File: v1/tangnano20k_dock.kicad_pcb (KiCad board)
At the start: 2 copper layers, 136.5 x 73.7 mm, 77 parts, among them J1 Mini-DIN-6, J10 DB15_Female_HighDensity_Mount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, J11 DB9_Male_MountingHoles, J12 DB9_Male_MountingHoles, J13 Conn_02x06_Odd_Even, J2 2x20 Pin Female, J3 Conn_01x20, J4 Conn_01x03_Male, J5 Conn_01x02, J6 RCA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

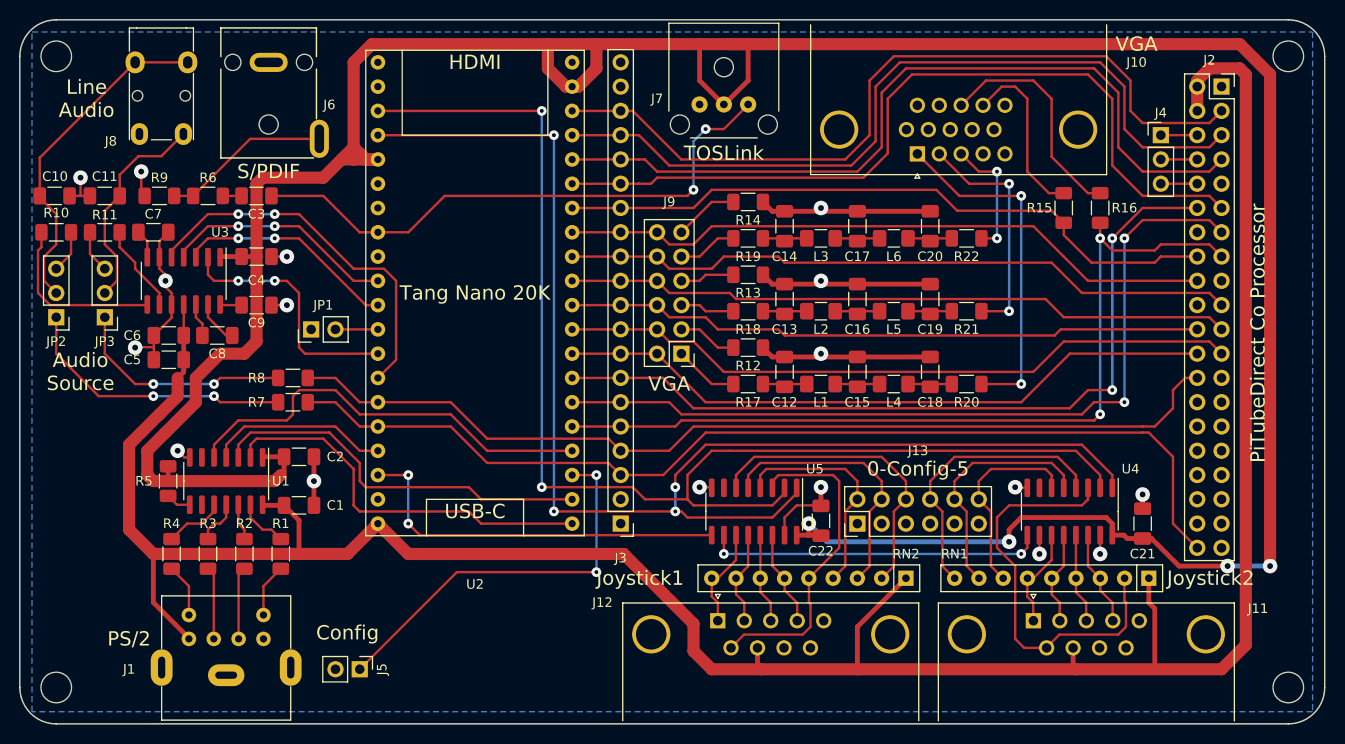
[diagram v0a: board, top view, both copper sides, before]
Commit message: Updated VGA jumper block from 2x6 to 3x6
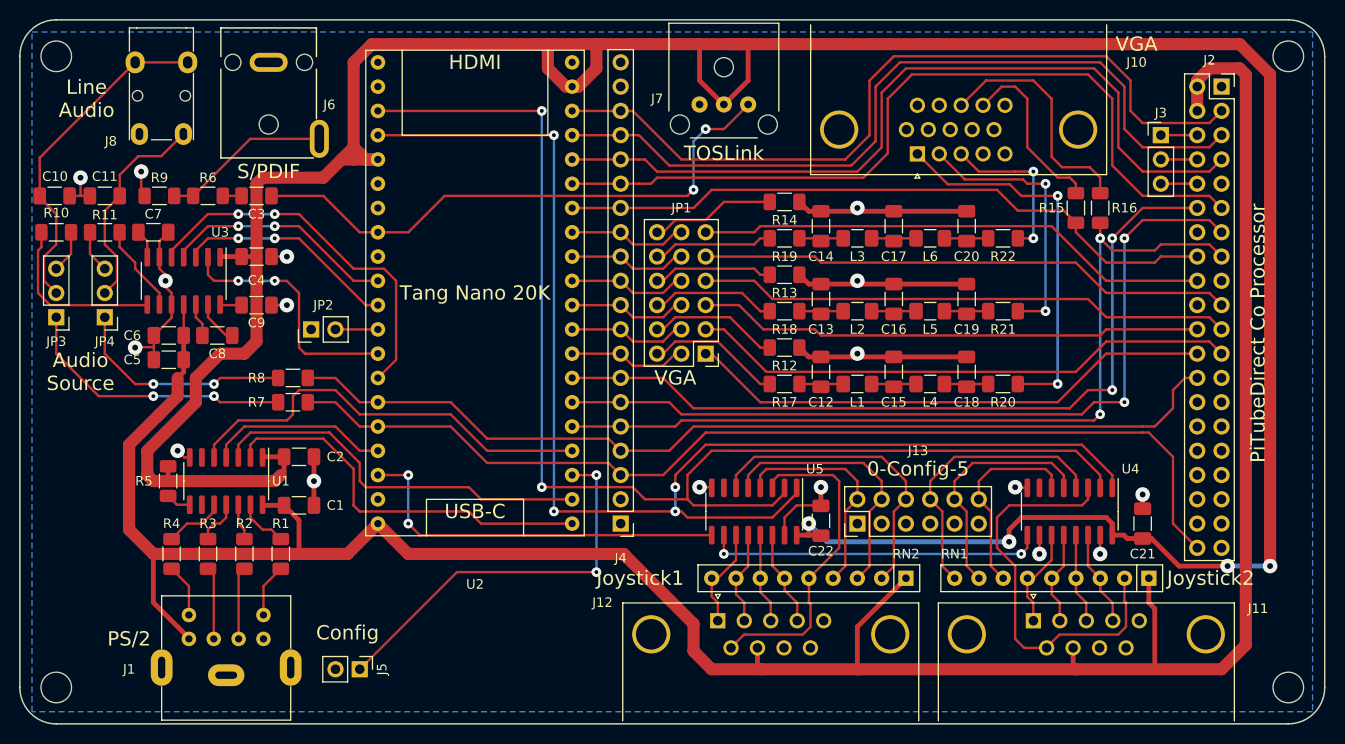
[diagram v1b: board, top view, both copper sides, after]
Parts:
- removed J9: Conn_02x06_Odd_Even, Connector_PinHeader_2.54mm:PinHeader_2x06_P2.54mm_Vertical
- added JP1: Jumper_03x06, TangNano20k:PinHeader_3x06_P2.54mm_Vertical, F.Cu at (144.8, 84.5)
- moved C12 3.81 mm to (156.8, 86.4)
- moved C13 3.81 mm to (156.8, 78.7)
- moved C14 3.81 mm to (156.8, 71.1)
- moved C15 3.81 mm to (164.5, 86.4)
- moved C16 3.81 mm to (164.5, 78.7)
- moved C17 3.81 mm to (164.5, 71.1)
- moved C18 3.81 mm to (172.1, 86.4)
- moved C19 3.81 mm to (172.1, 78.7)
- moved C20 3.81 mm to (172.1, 71.1)
- moved L1 3.81 mm to (160.7, 87.6)
- moved L2 3.81 mm to (160.7, 80.0)
- moved L3 3.81 mm to (160.7, 72.4)
- moved L4 3.81 mm to (168.3, 87.6)
- moved L5 3.81 mm to (168.3, 80.0)
- moved L6 3.81 mm to (168.3, 72.4)
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- renumbered J4 to J3, J3 to J4, JP1 to JP2, JP2 to JP3, JP3 to JP4
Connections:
- J2 pad 18: /VGA_B_n -> /DATA6
- J2 pad 19: /VGA_B -> /DATA2
- J2 pad 21: /VGA_G_n -> /DATA1
- J2 pad 22: /VGA_G -> /DATA7
- J2 pad 23: /VGA_R_n -> /DATA3
- J2 pad 24: /VGA_R -> /DATA0
- R12 pad 1: Net-(J9-Pad3) -> /VGA/VGA_R_n
- R13 pad 1: Net-(J9-Pad7) -> /VGA/VGA_G_n
- R14 pad 1: Net-(J9-Pad11) -> /VGA/VGA_B_n
- R17 pad 1: Net-(J9-Pad1) -> /VGA/VGA_R
- R18 pad 1: Net-(J9-Pad5) -> /VGA/VGA_G
- R19 pad 1: Net-(J9-Pad9) -> /VGA/VGA_B
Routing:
- net /VGA_R_n: track 71.6 -> 11.8 mm
- net /VGA_B: track 71.1 -> 11.8 mm
- net /VGA_R: track 69.6 -> 11.8 mm
- net /DATA3: track 0.00 -> 57.7 mm
- net /VGA_G_n: track 70.0 -> 12.5 mm
- net /VGA_B_n: track 69.1 -> 11.8 mm
- net /DATA2: track 0.00 -> 56.1 mm
- net /DATA1: track 0.00 -> 56.1 mm
- net /VGA_G: track 67.0 -> 11.8 mm
- net /DATA0: track 0.00 -> 55.0 mm
- net /DATA6: track 0.00 -> 54.1 mm
- net /DATA7: track 0.00 -> 53.0 mm
- net /VGA/VGA_R: track 0.00 -> 13.5 mm
- net /VGA/VGA_R_n: track 0.00 -> 13.0 mm
- net /VGA/VGA_B_n: track 0.00 -> 12.5 mm
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
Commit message: Updated VGA jumper block from 3x6 to 3x8
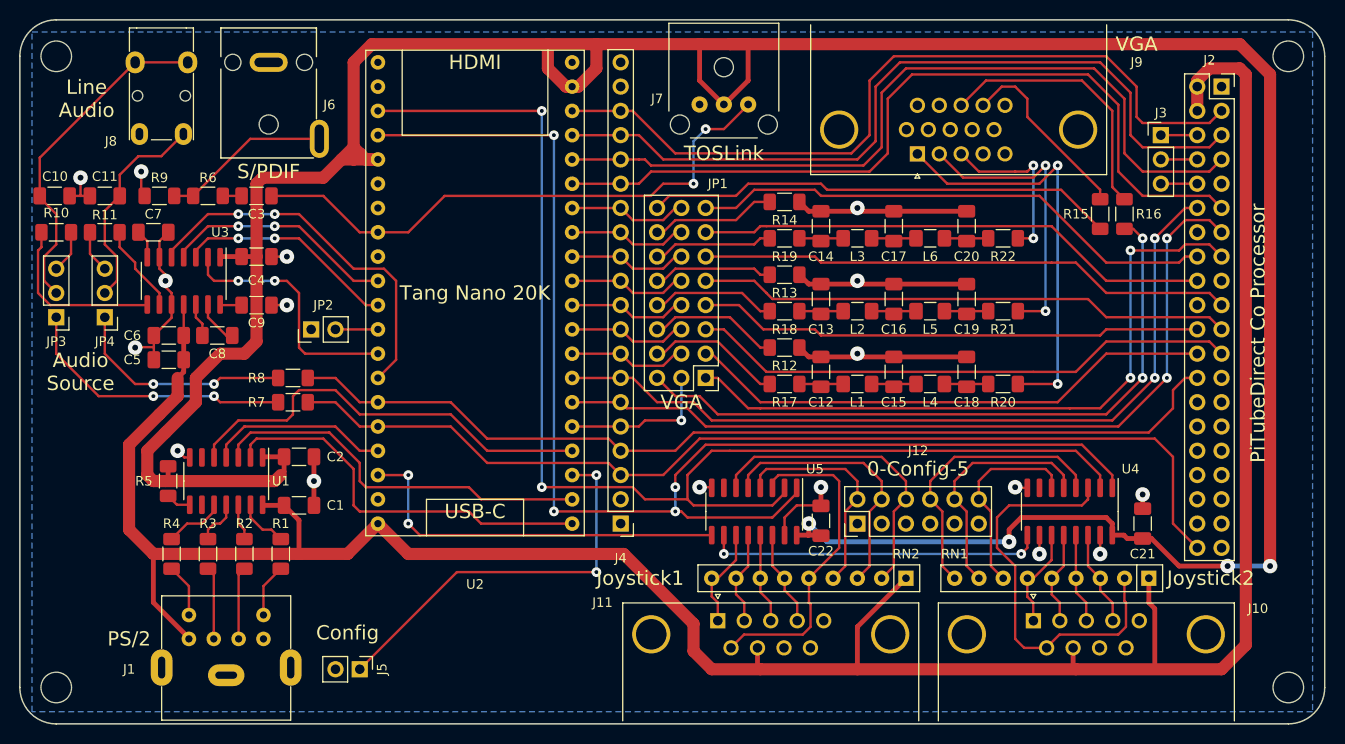
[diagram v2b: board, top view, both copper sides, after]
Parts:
- JP1: value Jumper_03x06 -> Jumper_03x08; footprint TangNano20k:PinHeader_3x06_P2.54mm_Vertical -> TangNano20k:PinHeader_3x08_P2.54mm_Vertical
- moved R15 2.62 mm to (186.1, 69.8)
- moved R16 2.62 mm to (188.6, 69.8)
- moved JP1 2.54 mm to (144.8, 87.0)
- renumbered J11 to J10, J12 to J11, J13 to J12, J10 to J9
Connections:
- J2 pad 15: /VGA_HS -> /DATA4
- J2 pad 16: /VGA_VS -> /DATA5
- JP1 pad 1: /DATA0 -> /DATA4
- JP1 pad 10: /VGA_G_n -> /VGA_R
- JP1 pad 11: /VGA_B -> /VGA_R_n
- JP1 pad 12: /VGA_B_n -> /VGA_G
- JP1 pad 13: /VGA/VGA_R -> /VGA_G_n
- JP1 pad 14: /VGA/VGA_R_n -> /VGA_B
- JP1 pad 15: /VGA/VGA_G -> /VGA_B_n
- JP1 pad 16: /VGA/VGA_G_n -> /VGA_VS
- JP1 pad 17: /VGA/VGA_B -> /VGA/VGA_HS
- JP1 pad 18: /VGA/VGA_B_n -> /VGA/VGA_R
- JP1 pad 2: /DATA3 -> /DATA0
- JP1 pad 3: /DATA7 -> /DATA3
- JP1 pad 4: /DATA1 -> /DATA7
- JP1 pad 5: /DATA2 -> /DATA1
- JP1 pad 6: /DATA6 -> /DATA2
- JP1 pad 7: /VGA_R -> /DATA6
- JP1 pad 8: /VGA_R_n -> /DATA5
- JP1 pad 9: /VGA_G -> /VGA_HS
- R15 pad 1: /VGA_VS -> /VGA/VGA_VS
- R16 pad 1: /VGA_HS -> /VGA/VGA_HS
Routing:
- net /VGA_HS: track 89.8 -> 16.1 mm, vias 2 -> 1
- net /VGA/VGA_HS: track 0.00 -> 70.9 mm, vias 0 -> 2
- net /DATA4: track 0.00 -> 70.7 mm, vias 0 -> 2
- net /VGA_VS: track 70.2 -> 11.8 mm
- net /DATA5: track 0.00 -> 55.6 mm
- net /VGA/VGA_VS: track 0.00 -> 49.4 mm
- net Net-(J9-Pad1): track 40.3 -> 43.8 mm
- net Net-(J9-Pad13): track 25.0 -> 28.0 mm
- net Net-(J9-Pad2): track 28.6 -> 30.8 mm
- net Net-(J9-Pad14): track 18.7 -> 19.6 mm
- net Net-(J9-Pad3): track 16.9 -> 17.8 mm
- net /VGA_G_n: track 12.5 -> 11.8 mm
- net /LED5: track 83.1 -> 82.6 mm
- net /LED3: track 84.6 -> 84.1 mm
- net /LED4: track 83.9 -> 83.4 mm
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
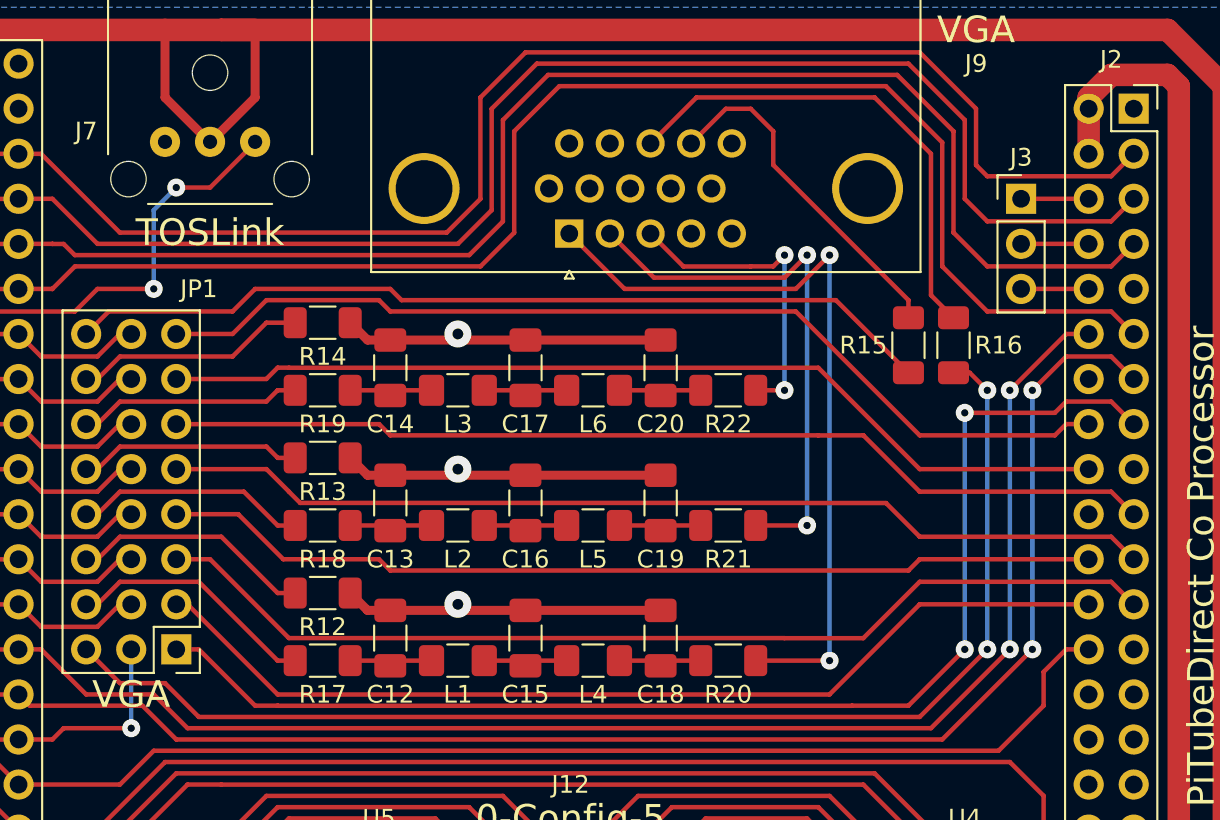
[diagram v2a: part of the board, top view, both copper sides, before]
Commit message: Spread out VGA filter passives
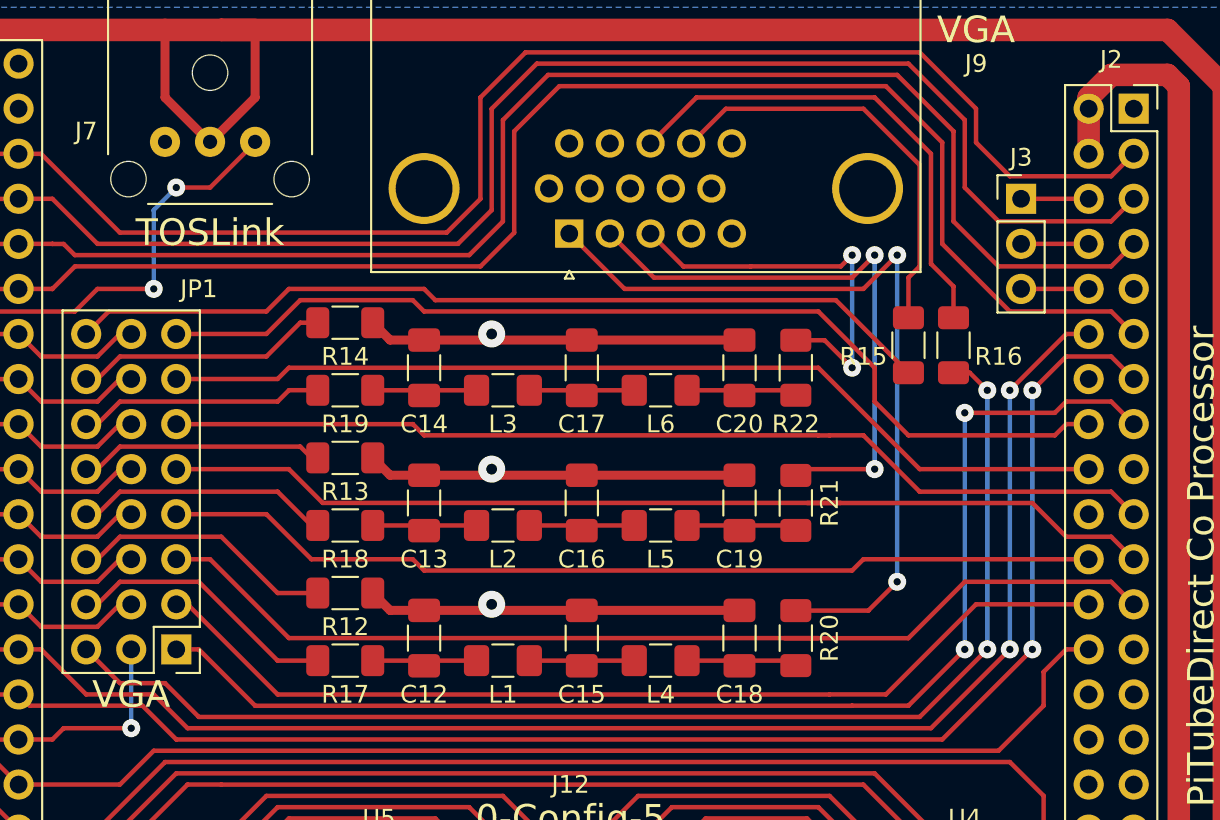
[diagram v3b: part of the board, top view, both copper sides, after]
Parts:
- moved C18 4.44 mm to (176.5, 86.4)
- moved C19 4.44 mm to (176.5, 78.7)
- moved C20 4.44 mm to (176.5, 71.1)
- moved R22 4.02 mm to (179.7, 71.1), turned to 90 degrees
- moved R20 4.02 mm to (179.7, 86.4), turned to 90 degrees
- moved R21 4.02 mm to (179.7, 78.7), turned to 90 degrees
- moved L4 3.81 mm to (172.1, 87.6)
- moved L5 3.81 mm to (172.1, 80.0)
- moved L6 3.81 mm to (172.1, 72.4)
- moved C15 3.17 mm to (167.6, 86.4)
- moved C16 3.17 mm to (167.6, 78.7)
- moved C17 3.17 mm to (167.6, 71.1)
- moved L1 2.54 mm to (163.2, 87.6)
- moved L2 2.54 mm to (163.2, 80.0)
- moved L3 2.54 mm to (163.2, 72.4)
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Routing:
- net GND: track 107.9 -> 117.4 mm
- net Net-(J9-Pad3): track 17.8 -> 22.6 mm
- net Net-(J9-Pad14): track 19.6 -> 23.9 mm
- net /DATA3: track 57.7 -> 59.6 mm
- net /DATA1: track 56.1 -> 58.0 mm
- net Net-(J9-Pad2): track 30.8 -> 32.6 mm
- net Net-(J9-Pad1): track 43.8 -> 45.4 mm
- net Net-(C14-Pad1): track 4.58 -> 5.85 mm
- net Net-(C13-Pad1): track 4.58 -> 5.85 mm
- net Net-(C12-Pad1): track 4.58 -> 5.85 mm
- net Net-(C20-Pad1): track 4.58 -> 5.85 mm
- net Net-(C19-Pad1): track 4.58 -> 5.85 mm
- net Net-(C18-Pad1): track 4.58 -> 5.85 mm
- net Net-(C17-Pad1): track 4.64 -> 5.91 mm
- net Net-(C16-Pad1): track 4.64 -> 5.91 mm
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
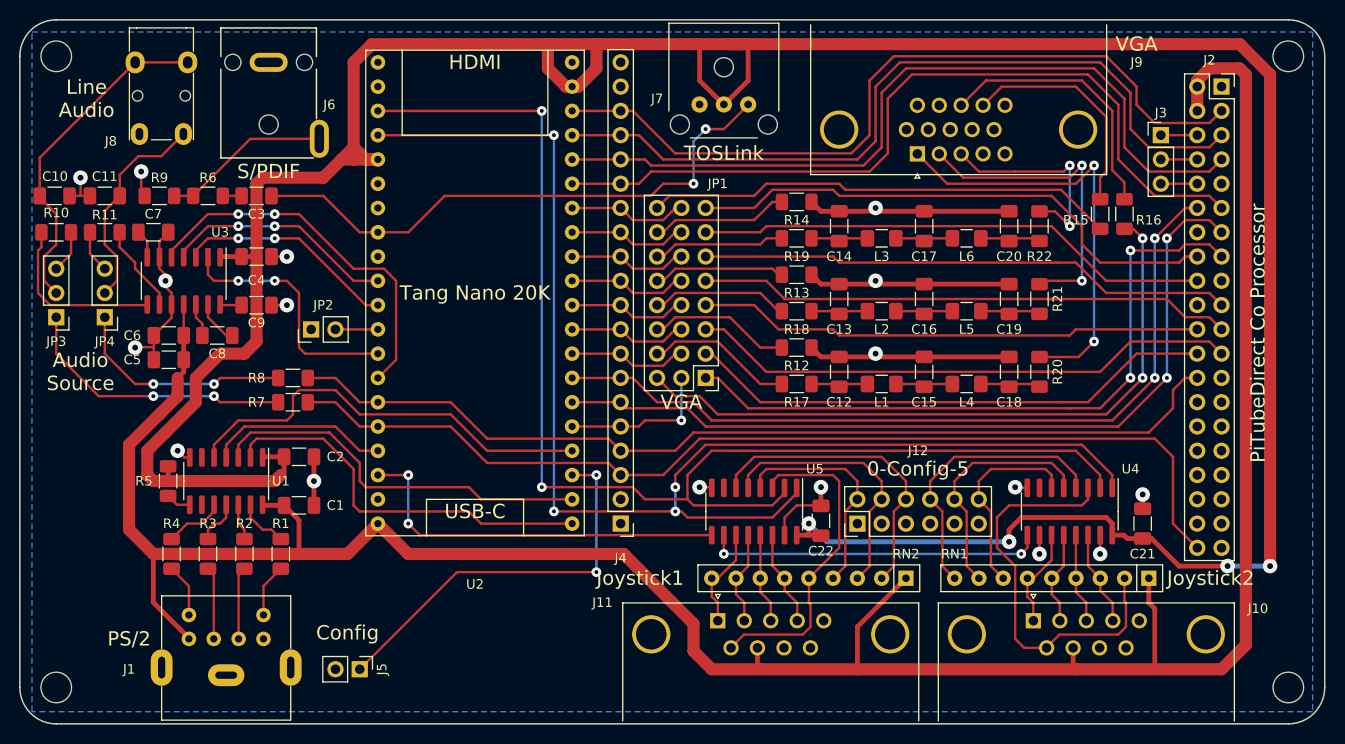
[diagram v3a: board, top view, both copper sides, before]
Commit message: Spread out audio passives
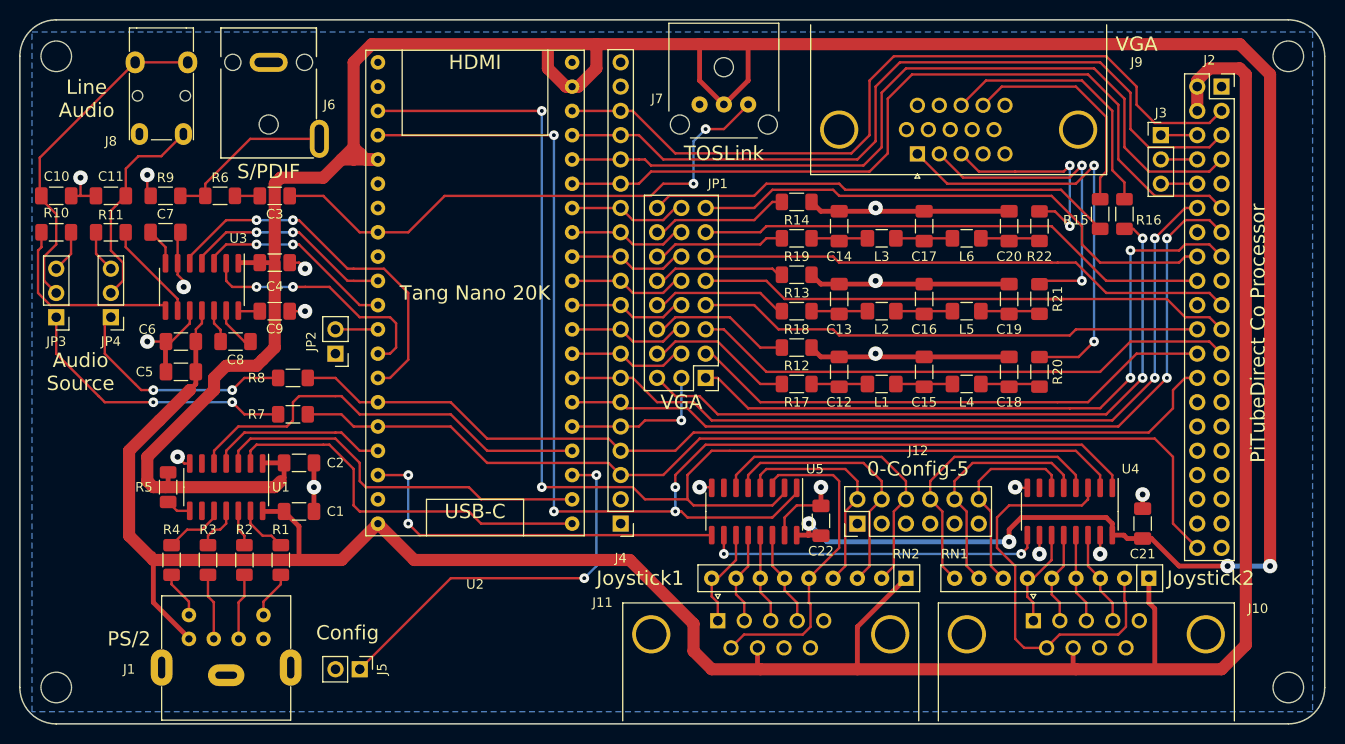
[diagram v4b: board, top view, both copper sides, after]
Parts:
- moved JP2 3.59 mm to (106.0, 84.5), turned to 180 degrees
- moved C8 2.01 mm to (95.6, 83.2)
- moved U3 2.01 mm to (92.1, 77.5)
- moved C4 2.01 mm to (99.7, 74.9)
- moved C9 2.01 mm to (99.7, 80.0)
- moved C3 1.90 mm to (99.7, 67.9)
- moved C5 1.79 mm to (89.9, 86.4)
- moved C6 1.42 mm to (89.9, 83.2)
- moved R6 1.27 mm to (94.0, 67.9)
- moved C7 1.27 mm to (88.3, 71.8)
- moved R7 1.27 mm to (101.6, 90.8)
- moved R9 0.64 mm to (88.3, 67.9)
- moved C11 0.64 mm to (82.5, 67.9)
- moved JP4 0.64 mm to (82.5, 80.6)
- moved R1 0.64 mm to (100.3, 106.0)
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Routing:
- net /I2S_MCLK: track 22.5 -> 20.3 mm
- net /I2S_LRCLK: track 23.7 -> 21.6 mm
- net Net-(R10-Pad2): track 18.4 -> 20.3 mm
- net /SPDIF: track 59.6 -> 57.7 mm
- net Net-(R11-Pad2): track 9.28 -> 10.4 mm
- net +5V: track 267.4 -> 268.4 mm
- net Net-(C7-Pad1): track 2.99 -> 3.89 mm
- net GND: track 117.4 -> 116.6 mm
- net +3.3V: track 324.6 -> 323.8 mm
- net Net-(J1-Pad1): track 7.59 -> 6.94 mm
- net Net-(J1-Pad6): track 5.59 -> 4.96 mm
- net Net-(J1-Pad5): track 5.59 -> 4.96 mm
- net Net-(C3-Pad2): track 1.97 -> 2.60 mm
- net Net-(J1-Pad2): track 7.59 -> 6.97 mm
- net /RC_AUDIO_R: track 29.1 -> 29.7 mm
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
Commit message: Silk screen
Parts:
- moved J5 6.48 mm to (107.3, 111.1)
- renumbered J12 to JP5
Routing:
- net /KBD_CONFIG_MODIFIER: track 41.3 -> 39.9 mm
- net Net-(J9-Pad3): track 22.6 -> 23.4 mm
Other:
- board text added: "Debug"
- board text added: "Serial"
- board text added: "VGA/PiTube"
